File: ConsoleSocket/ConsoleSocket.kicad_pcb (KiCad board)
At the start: 2 copper layers, 95 x 15.2 mm, 4 parts, among them J1 Conn_01x05_Male, J3 Conn_02x25_Odd_Even

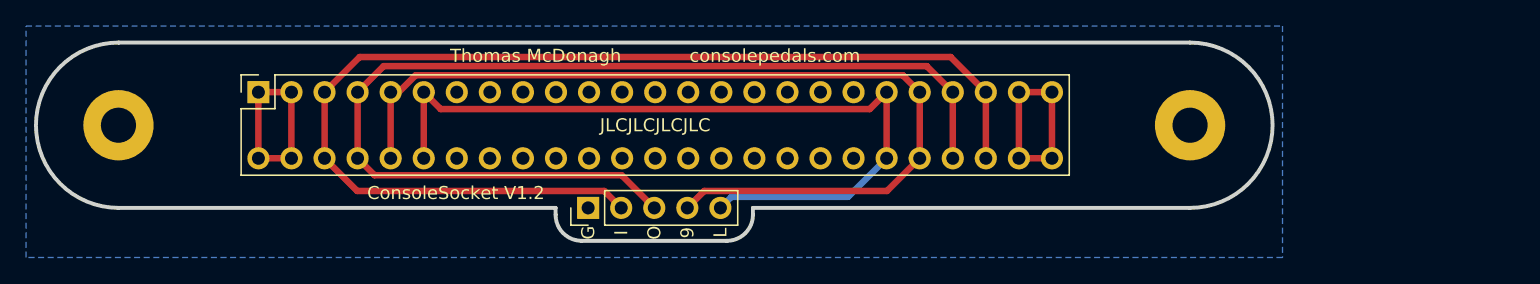
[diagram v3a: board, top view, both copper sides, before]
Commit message: Added switched connection for 9V
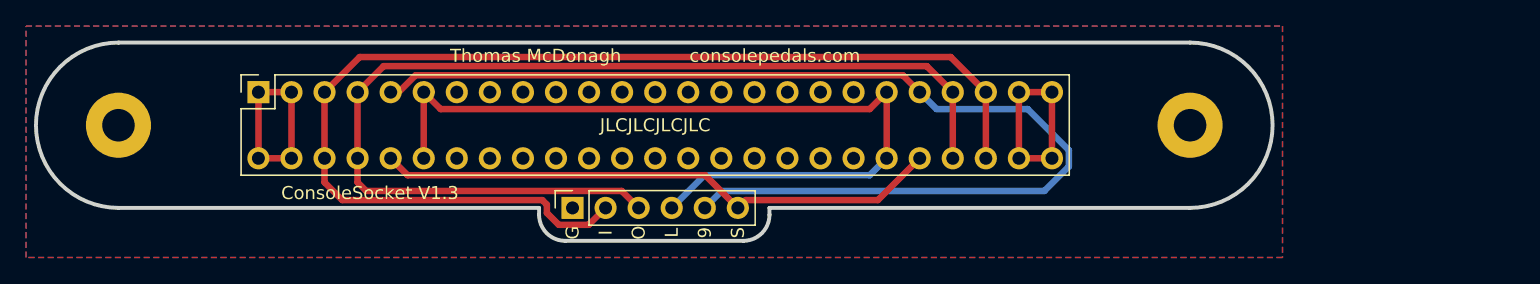
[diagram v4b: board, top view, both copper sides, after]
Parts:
- H1, H2: footprint MountingHole:MountingHole_2.7mm_Pad -> MountingHole:MountingHole_2.5mm_Pad
- J1: value Conn_01x05_Male -> Conn; footprint Connector_PinHeader_2.54mm:PinHeader_1x05_P2.54mm_Vertical -> Connector_PinSocket_2.54mm:PinSocket_1x06_P2.54mm_Vertical
- moved J1 1.20 mm to (130.9, 45.7)
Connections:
- J1 pad 4: +9V -> /LEDPower
- J1 pad 5: /LEDPower -> +9V
- J3 pad 10: +9V -> /SW
- J3 pad 42: +9V -> /SW
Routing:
- net /SW: track 0.00 -> 43.8 mm
- net +9V: track 71.9 -> 85.6 mm
- net /LEDPower: track 61.8 -> 65.5 mm
- net /Input: track 88.2 -> 89.5 mm
- added copper zone on F.Cu, net GND
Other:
- outline, holes or cut-outs redrawn
- board text added: "ConsoleSocket V1.3"
- board text added: "S"
- board text removed: "ConsoleSocket V1.2"

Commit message: Widened pin header holes for easier hand soldering
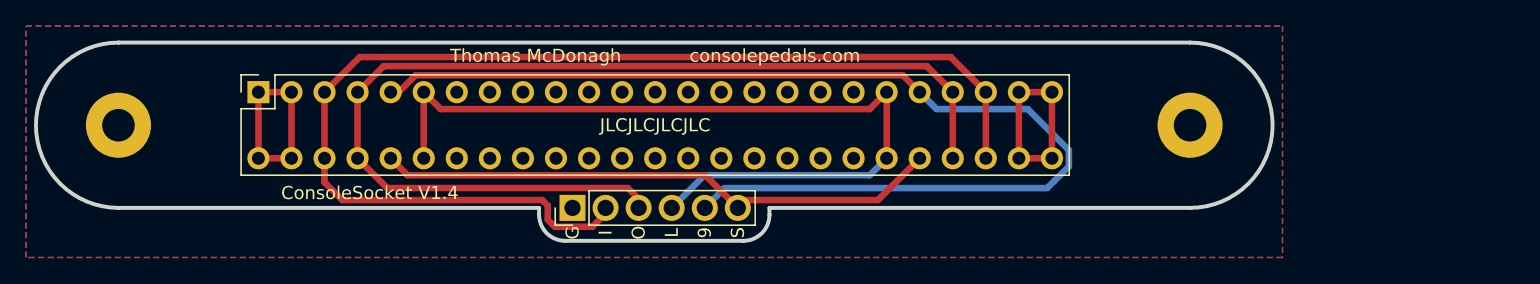
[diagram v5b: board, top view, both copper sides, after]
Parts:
- J1: footprint Connector_PinSocket_2.54mm:PinSocket_1x06_P2.54mm_Vertical -> libraries:Pins_1x06_Wide
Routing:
- net /Output: track 81.8 -> 81.1 mm
- net /Input: track 89.5 -> 90.2 mm
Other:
- board text added: "ConsoleSocket V1.4"
- board text removed: "ConsoleSocket V1.3"
